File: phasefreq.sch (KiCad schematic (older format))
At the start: 98 parts, among them J1 Power Input, J2 RF Input, J3 LO Input, J4 VCO Tune, U1 LM317_3PinPackage, U2 LM337_SOT223, U3 ADCMP564, U4 AD9901, U5 LM4040DBZ-3, U6 AD8676, U7 AD8676

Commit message: notations for future work
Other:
- note added: "Clean up bypass cap situation here?"
- note added: "Switch to ADCMP565? Better package (same as PFD), maybe more complicated hysteresis?"
- note added: "VTUNE- is wrong. switch to LM4040-2.5 or tune op-amp resistors?"
- note added: "What is going on at this termination again?\nReplace with termination to 50 Ohm to ground?"
- note removed: "VTUNE- is wrong. set both to 2.5 (different LM4040-X, or tune R?)"
- moved on the sheet: C33, C35, R14, R17, R18, R20, R21, R22
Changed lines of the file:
@@
 	-1   0    0    1
 $EndComp
-Text GLabel 5450 1450 0    50   Input ~ 0
+Text GLabel 5800 1450 0    50   Input ~ 0
 PFD_OUT
-Text GLabel 5450 1750 0    50   Input ~ 0
+Text GLabel 5800 1750 0    50   Input ~ 0
 ~PFD_OUT~
 $Comp
 L Device:R R14
 U 1 1 5CEF1598
-P 5700 1600
-F 0 "R14" H 5770 1646 50  0000 L CNN
-F 1 "182" H 5770 1555 50  0000 L CNN
-F 2 "Resistor_SMD:R_0603_1608Metric" V 5630 1600 50  0001 C CNN
-F 3 "~" H 5700 1600 50  0001 C CNN
-	1    5700 1600
-	1    0    0    -1
-$EndComp
-Wire Wire Line
-	5450 1450 5700 1450
-Wire Wire Line
-	5450 1750 5700 1750
+P 6050 1600
+F 0 "R14" H 6120 1646 50  0000 L CNN
+F 1 "182" H 6120 1555 50  0000 L CNN
+F 2 "Resistor_SMD:R_0603_1608Metric" V 5980 1600 50  0001 C CNN
+F 3 "~" H 6050 1600 50  0001 C CNN
+	1    6050 1600
+	1    0    0    -1
+$EndComp
+Wire Wire Line
+	5800 1450 6050 1450
+Wire Wire Line
+	5800 1750 6050 1750
 $Comp
 L Device:R_Small R18
 U 1 1 5CEFCB9E
-P 6400 1750
-F 0 "R18" V 6204 1750 50  0000 C CNN
-F 1 "10K" V 6300 1750 50  0000 C CNN
-F 2 "Resistor_SMD:R_0603_1608Metric" H 6400 1750 50  0001 C CNN
-F 3 "~" H 6400 1750 50  0001 C CNN
-	1    6400 1750
+P 6750 1750
+F 0 "R18" V 6554 1750 50  0000 C CNN
+F 1 "10K" V 6650 1750 50  0000 C CNN
+F 2 "Resistor_SMD:R_0603_1608Metric" H 6750 1750 50  0001 C CNN
+F 3 "~" H 6750 1750 50  0001 C CNN
+	1    6750 1750
 	0    1    1    0
 $EndComp
@@
 L Device:R_Small R20
 U 1 1 5CEFD5C0
-P 6600 1950
-F 0 "R20" H 6541 1904 50  0000 R CNN
-F 1 "0R0" H 6541 1995 50  0000 R CNN
-F 2 "Resistor_SMD:R_0603_1608Metric" H 6600 1950 50  0001 C CNN
-F 3 "~" H 6600 1950 50  0001 C CNN
-	1    6600 1950
+P 6950 1950
+F 0 "R20" H 6891 1904 50  0000 R CNN
+F 1 "0R0" H 6891 1995 50  0000 R CNN
+F 2 "Resistor_SMD:R_0603_1608Metric" H 6950 1950 50  0001 C CNN
+F 3 "~" H 6950 1950 50  0001 C CNN
+	1    6950 1950
 	-1   0    0    1
 $EndComp
@@
 L Device:C_Small C33
 U 1 1 5CEFDFB8
-P 6600 2150
-F 0 "C33" H 6692 2196 50  0000 L CNN
-F 1 "100n" H 6692 2105 50  0000 L CNN
-F 2 "Capacitor_SMD:C_0603_1608Metric" H 6600 2150 50  0001 C CNN
-F 3 "~" H 6600 2150 50  0001 C CNN
-	1    6600 2150
+P 6950 2150
+F 0 "C33" H 7042 2196 50  0000 L CNN
+F 1 "100n" H 7042 2105 50  0000 L CNN
+F 2 "Capacitor_SMD:C_0603_1608Metric" H 6950 2150 50  0001 C CNN
+F 3 "~" H 6950 2150 50  0001 C CNN
+	1    6950 2150
 	1    0    0    -1
 $EndComp
@@
 L power:GNDA #PWR021
 U 1 1 5CEFECFC
-P 6600 2250
-F 0 "#PWR021" H 6600 2000 50  0001 C CNN
-F 1 "GNDA" H 6605 2077 50  0000 C CNN
-F 2 "" H 6600 2250 50  0001 C CNN
-F 3 "" H 6600 2250 50  0001 C CNN
-	1    6600 2250
-	1    0    0    -1
-$EndComp
-Wire Wire Line
-	6500 1750 6600 1750
-Wire Wire Line
-	6600 1750 6600 1850
+P 6950 2250
+F 0 "#PWR021" H 6950 2000 50  0001 C CNN
+F 1 "GNDA" H 6955 2077 50  0000 C CNN
+F 2 "" H 6950 2250 50  0001 C CNN
+F 3 "" H 6950 2250 50  0001 C CNN
+	1    6950 2250
+	1    0    0    -1
+$EndComp
+Wire Wire Line
+	6850 1750 6950 1750
+Wire Wire Line
+	6950 1750 6950 1850
 Wire Notes Line
-	6250 2600 6250 1450
-Text Notes 7000 2750 2    50   ~ 0
+	6600 2600 6600 1450
+Text Notes 7350 2750 2    50   ~ 0
 Loop filter
 Wire Wire Line
@@
 L Device:R_Small R17
 U 1 1 5CF043BB
-P 5850 1450
-F 0 "R17" V 5654 1450 50  0000 C CNN
-F 1 "0R0" V 5745 1450 50  0000 C CNN
-F 2 "Resistor_SMD:R_0603_1608Metric" H 5850 1450 50  0001 C CNN
-F 3 "~" H 5850 1450 50  0001 C CNN
-	1    5850 1450
+P 6200 1450
+F 0 "R17" V 6004 1450 50  0000 C CNN
+F 1 "0R0" V 6095 1450 50  0000 C CNN
+F 2 "Resistor_SMD:R_0603_1608Metric" H 6200 1450 50  0001 C CNN
+F 3 "~" H 6200 1450 50  0001 C CNN
+	1    6200 1450
 	0    1    1    0
 $EndComp
@@
 L power:GNDA #PWR020
 U 1 1 5CF425BE
-P 6100 1500
-F 0 "#PWR020" H 6100 1250 50  0001 C CNN
-F 1 "GNDA" H 6105 1327 50  0000 C CNN
-F 2 "" H 6100 1500 50  0001 C CNN
-F 3 "" H 6100 1500 50  0001 C CNN
-	1    6100 1500
-	1    0    0    -1
-$EndComp
-Wire Wire Line
-	5700 1450 5750 1450
-Connection ~ 5700 1450
-Wire Wire Line
-	6100 1450 6100 1500
+P 6450 1500
+F 0 "#PWR020" H 6450 1250 50  0001 C CNN
+F 1 "GNDA" H 6455 1327 50  0000 C CNN
+F 2 "" H 6450 1500 50  0001 C CNN
+F 3 "" H 6450 1500 50  0001 C CNN
+	1    6450 1500
+	1    0    0    -1
+$EndComp
+Wire Wire Line
+	6050 1450 6100 1450
+Connection ~ 6050 1450
+Wire Wire Line
+	6450 1450 6450 1500
 $Comp
 L Connector:Conn_Coaxial J3
@@
 $EndComp
 Wire Wire Line
-	5950 1450 6100 1450
+	6300 1450 6450 1450
 $Comp
 L power:PWR_FLAG #FLG03
@@
 L Device:R_Small R21
 U 1 1 5E2D216E
-P 6850 1750
-F 0 "R21" V 6654 1750 50  0000 C CNN
-F 1 "0R0" V 6750 1750 50  0000 C CNN
-F 2 "Resistor_SMD:R_0603_1608Metric" H 6850 1750 50  0001 C CNN
-F 3 "~" H 6850 1750 50  0001 C CNN
-	1    6850 1750
+P 7200 1750
+F 0 "R21" V 7004 1750 50  0000 C CNN
+F 1 "0R0" V 7100 1750 50  0000 C CNN
+F 2 "Resistor_SMD:R_0603_1608Metric" H 7200 1750 50  0001 C CNN
+F 3 "~" H 7200 1750 50  0001 C CNN
+	1    7200 1750
 	0    1    1    0
 $EndComp
@@
 L Device:R_Small R22
 U 1 1 5E2D2174
-P 7050 1950
-F 0 "R22" H 6991 1904 50  0000 R CNN
-F 1 "DNP" H 6991 1995 50  0000 R CNN
-F 2 "Resistor_SMD:R_0603_1608Metric" H 7050 1950 50  0001 C CNN
-F 3 "~" H 7050 1950 50  0001 C CNN
-	1    7050 1950
+P 7400 1950
+F 0 "R22" H 7341 1904 50  0000 R CNN
+F 1 "DNP" H 7341 1995 50  0000 R CNN
+F 2 "Resistor_SMD:R_0603_1608Metric" H 7400 1950 50  0001 C CNN
+F 3 "~" H 7400 1950 50  0001 C CNN
+	1    7400 1950
 	-1   0    0    1
 $EndComp
@@
 L Device:C_Small C35
 U 1 1 5E2D217A
-P 7050 2150
-F 0 "C35" H 7142 2196 50  0000 L CNN
-F 1 "DNP" H 7142 2105 50  0000 L CNN
-F 2 "Capacitor_SMD:C_0603_1608Metric" H 7050 2150 50  0001 C CNN
-F 3 "~" H 7050 2150 50  0001 C CNN
-	1    7050 2150
+P 7400 2150
+F 0 "C35" H 7492 2196 50  0000 L CNN
+F 1 "DNP" H 7492 2105 50  0000 L CNN
+F 2 "Capacitor_SMD:C_0603_1608Metric" H 7400 2150 50  0001 C CNN
+F 3 "~" H 7400 2150 50  0001 C CNN
+	1    7400 2150
 	1    0    0    -1
 $EndComp
@@
 L power:GNDA #PWR024
 U 1 1 5E2D2180
-P 7050 2250
-F 0 "#PWR024" H 7050 2000 50  0001 C CNN
-F 1 "GNDA" H 7055 2077 50  0000 C CNN
-F 2 "" H 7050 2250 50  0001 C CNN
-F 3 "" H 7050 2250 50  0001 C CNN
-	1    7050 2250
-	1    0    0    -1
-$EndComp
-Wire Wire Line
-	6950 1750 7050 1750
-Wire Wire Line
-	7050 1750 7050 1850
+P 7400 2250
+F 0 "#PWR024" H 7400 2000 50  0001 C CNN
+F 1 "GNDA" H 7405 2077 50  0000 C CNN
+F 2 "" H 7400 2250 50  0001 C CNN
+F 3 "" H 7400 2250 50  0001 C CNN
+	1    7400 2250
+	1    0    0    -1
+$EndComp
+Wire Wire Line
+	7300 1750 7400 1750
+Wire Wire Line
+	7400 1750 7400 1850
 Wire Notes Line
-	6250 1450 7350 1450
+	6600 1450 7700 1450
 Wire Notes Line
-	7350 1450 7350 2600
+	7700 1450 7700 2600
 Wire Notes Line
-	7350 2600 6250 2600
-Wire Wire Line
-	5700 1750 6300 1750
-Connection ~ 5700 1750
-Wire Wire Line
-	6600 1750 6750 1750
-Connection ~ 6600 1750
-Wire Wire Line
-	7050 1750 7900 1750
-Connection ~ 7050 1750
+	7700 2600 6600 2600
+Wire Wire Line
+	6050 1750 6650 1750
+Connection ~ 6050 1750
+Wire Wire Line
+	6950 1750 7100 1750
+Connection ~ 6950 1750
 $Comp
 L Device:C_Small C41
@@
 ADCMP564 input voltage range: -2 V to 3 V
 Text Notes 8600 4000 0    50   ~ 0
-VTUNE- is wrong. set both to 2.5 (different LM4040-X, or tune R?)
+VTUNE- is wrong. switch to LM4040-2.5 or tune op-amp resistors?
 $Comp
 L grav:SLVU2.8-8 D?
@@
 Wire Wire Line
 	3600 1450 3600 1550
+Wire Wire Line
+	7400 1750 7900 1750
+Connection ~ 7400 1750
+Text Notes 5650 6300 0    50   ~ 0
+Clean up bypass cap situation here?
+Text Notes 5300 1100 0    50   ~ 0
+What is going on at this termination again?\nReplace with termination to 50 Ohm to ground?
+Text Notes 4750 2600 0    50   ~ 0
+Switch to ADCMP565? Better package (same as PFD), maybe more complicated hysteresis?
 $EndSCHEMATC

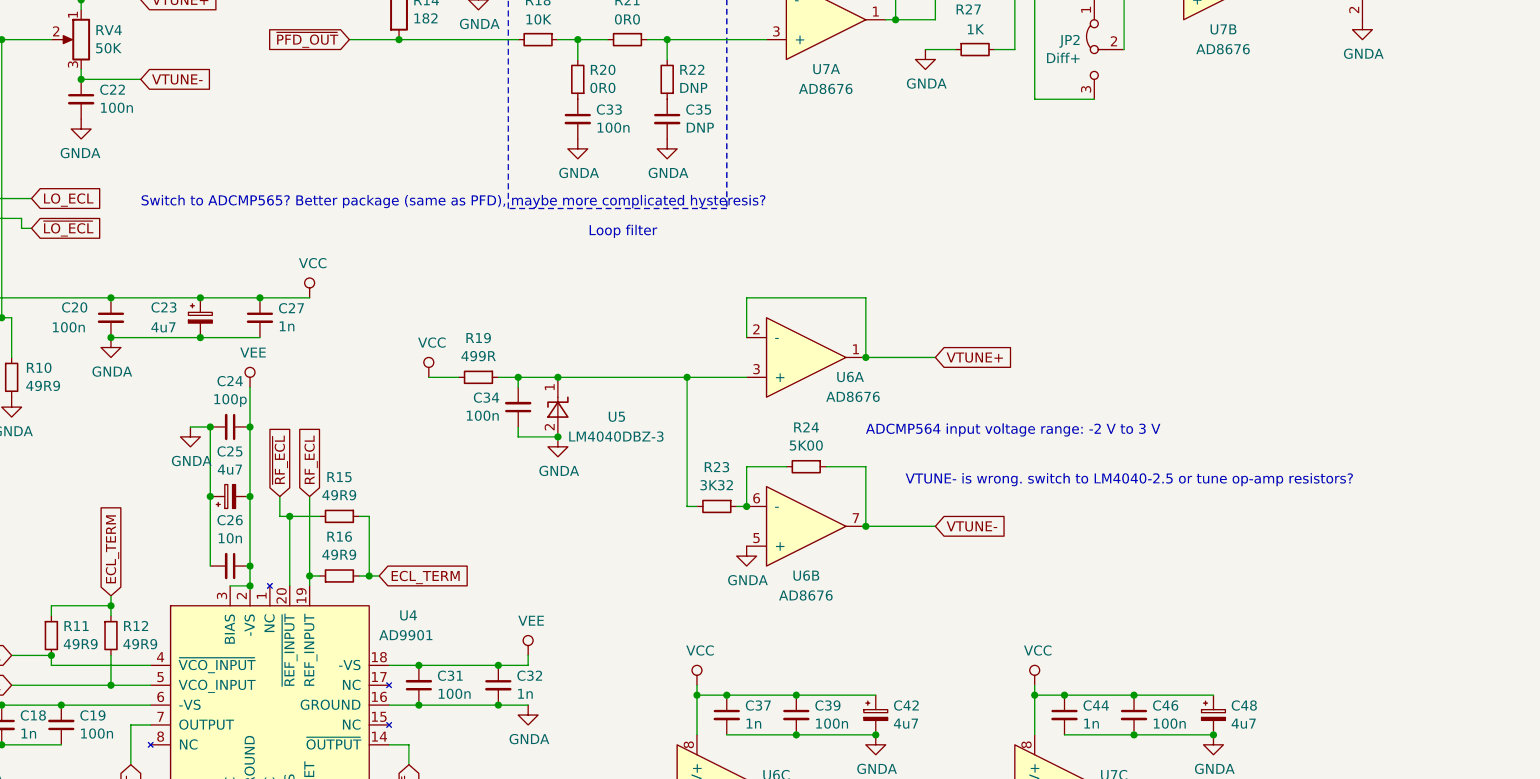
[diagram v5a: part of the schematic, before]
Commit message: added ADCMP565 component, sch annotations for future changes
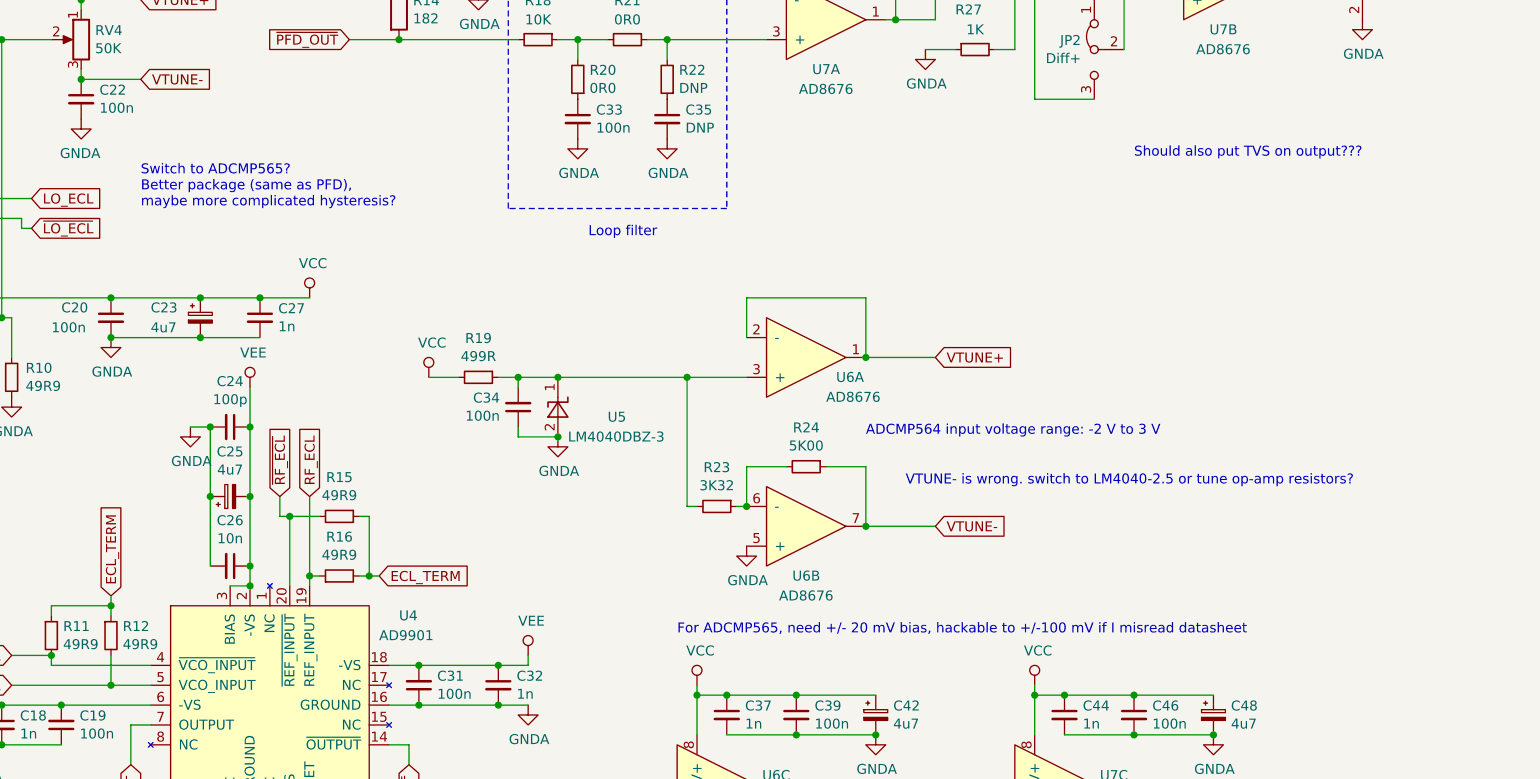
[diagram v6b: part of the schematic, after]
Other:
- note added: "For ADCMP565, need +/- 20 mV bias, hackable to +/-100 mV if I misread datasheet"
- note added: "Should also put TVS on output???"
- note added: "Switch to ADCMP565?\nBetter package (same as PFD),\nmaybe more complicated hysteresis?"
- note removed: "Switch to ADCMP565? Better package (same as PFD), maybe more complicated hysteresis?"
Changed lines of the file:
@@
 What is going on at this termination again?\nReplace with termination to 50 Ohm to ground?
 Text Notes 4750 2600 0    50   ~ 0
-Switch to ADCMP565? Better package (same as PFD), maybe more complicated hysteresis?
+Switch to ADCMP565?\nBetter package (same as PFD),\nmaybe more complicated hysteresis?
+Text Notes 7450 4750 0    50   ~ 0
+For ADCMP565, need +/- 20 mV bias, hackable to +/-100 mV if I misread datasheet
+Text Notes 9750 2350 0    50   ~ 0
+Should also put TVS on output???
 $EndSCHEMATC

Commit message: cleaned up bypass caps, comp for new adcmp
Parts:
- removed C24, C30: 100p, Capacitor_SMD:C_0603_1608Metric, symbol Device:C_Small
- removed C27, C7: 1n, Capacitor_SMD:C_0603_1608Metric, symbol Device:C_Small
- C18: value 1n -> 10n
- C19: value 100n -> 1u; symbol Device:C_Small -> Device:CP_Small
- C20, C31, C9: value 100n -> 10n
- C23, C25, C29, C8: value 4u7 -> 1u
- C32: value 1n -> 1u; symbol Device:C_Small -> Device:CP_Small
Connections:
- net GNDA: now also C32.1; no longer C32.2
- net VEE: now also C32.2; no longer C32.1
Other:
- note added: "ADCMP564 input voltage range: -2 V to 3 V\nTVS diodes: +/-2.8 V\n-2.8 is within maximum permissible voltage"
- note removed: "ADCMP564 input voltage range: -2 V to 3 V"
- note removed: "Clean up bypass cap situation here?"
- moved on the sheet: C16, C17, C18, C25, C26, RV2, RV3

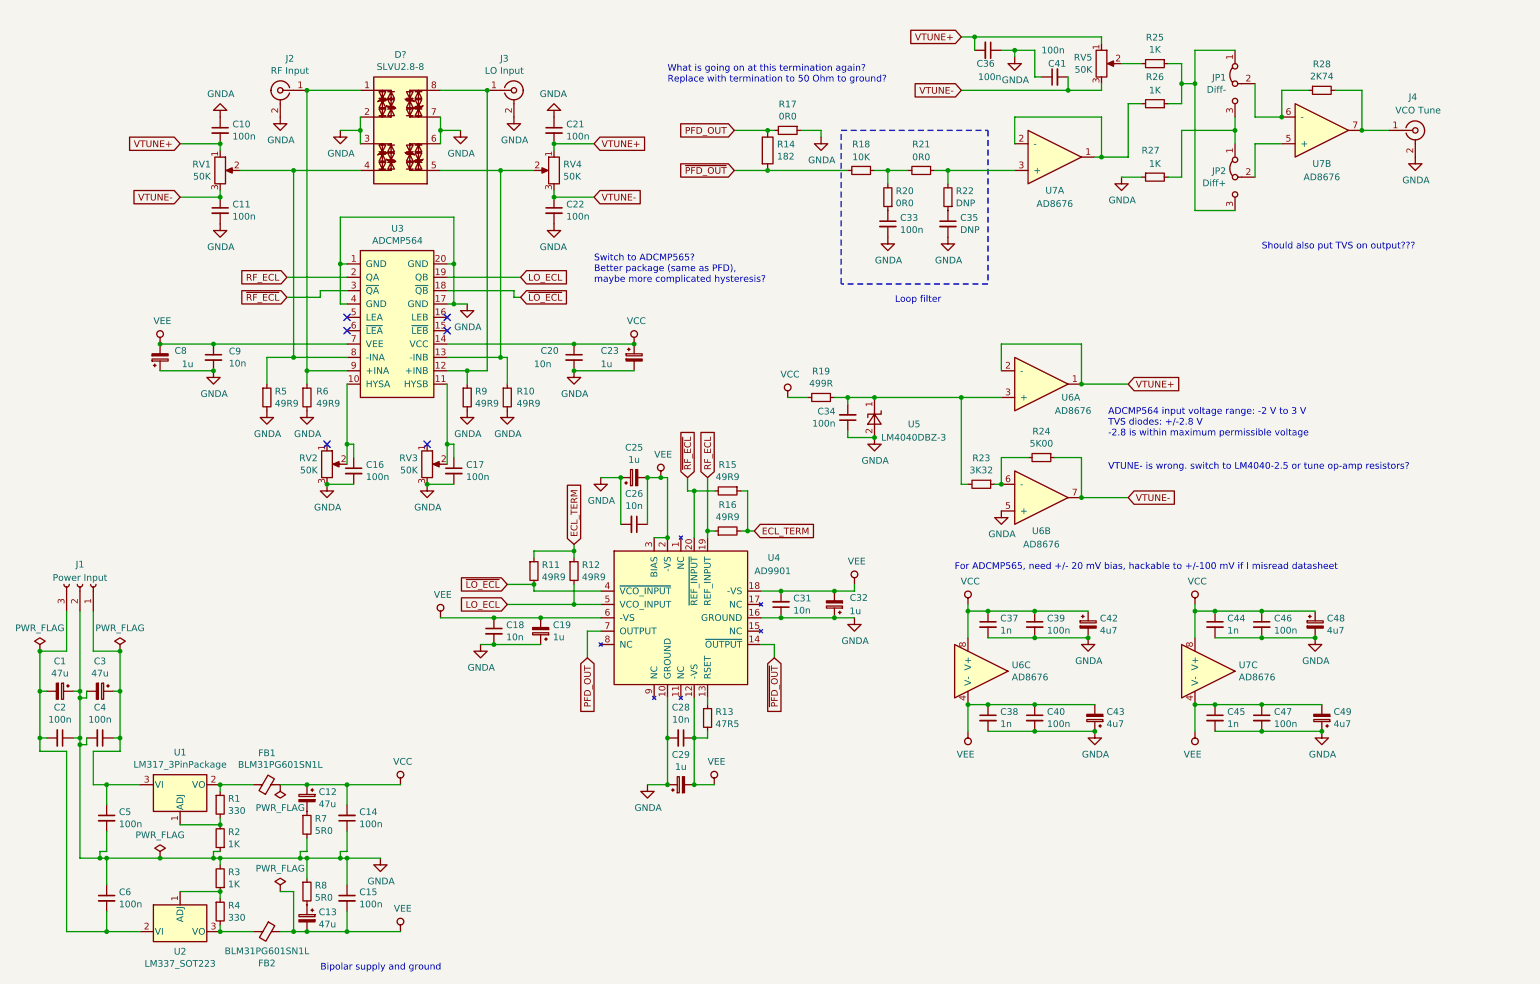
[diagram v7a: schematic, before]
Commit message: cleaned up loop filter (up to 3rd order possible) and subs. gain stages
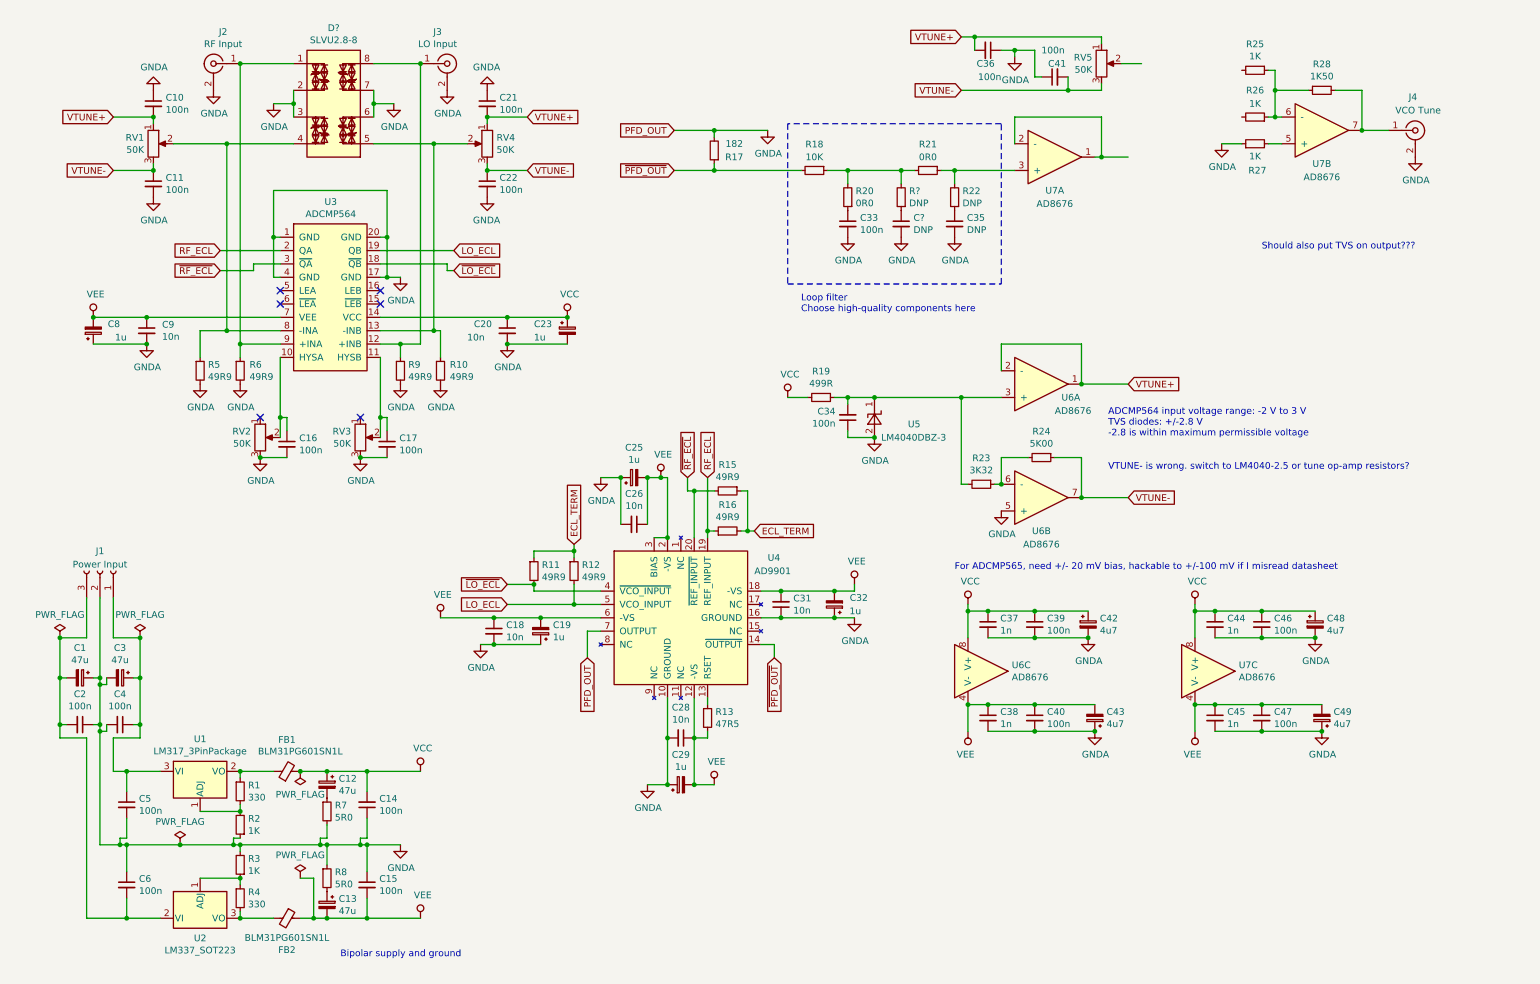
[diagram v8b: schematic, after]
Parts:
- removed JP1: Diff-, symbol Jumper:Jumper_3_Bridged12
- removed JP2: Diff+, symbol Jumper:Jumper_3_Bridged12
- removed R14: 182, Resistor_SMD:R_0603_1608Metric, symbol Device:R
- added C?: DNP, Capacitor_SMD:C_0603_1608Metric, symbol Device:C_Small
- added R?: DNP, Resistor_SMD:R_0603_1608Metric, symbol Device:R_Small
- R17: value 0R0 -> 182
- R28: value 2K74 -> 1K50
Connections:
- net PFD_OUT is gone; now on net GNDA: R17.2, U4.7 (OUTPUT)
- net GNDA: now also C?.2; no longer R17.1
- net ~PFD_OUT~: now also R17.1
- net at R18.1, R20.2, R21.2: now also R?.2
- net at R28.1, U7.6 (-): now also R25.1, R26.1
- net at R27.2: now also U7.5 (+)
- net at U7.1, U7.2 (-): no longer R26.2
- net at R25.2: no longer RV5.2
- new net: C?.1, R?.1
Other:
- note added: "Loop filter\nChoose high-quality components here\n\n"
- note removed: "Loop filter"
- note removed: "Switch to ADCMP565?\nBetter package (same as PFD),\nmaybe more complicated hysteresis?"
- note removed: "What is going on at this termination again?\nReplace with termination to 50 Ohm to ground?"
- moved on the sheet: C1, C10, C11, C12, C13, C14, C15, C16, C17, C2, C20, C21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
